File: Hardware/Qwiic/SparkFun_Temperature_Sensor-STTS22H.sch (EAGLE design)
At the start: 28 parts, among them J1 QWIIC_RIGHT_ANGLE, J2 QWIIC_RIGHT_ANGLE, U2 STTS22H

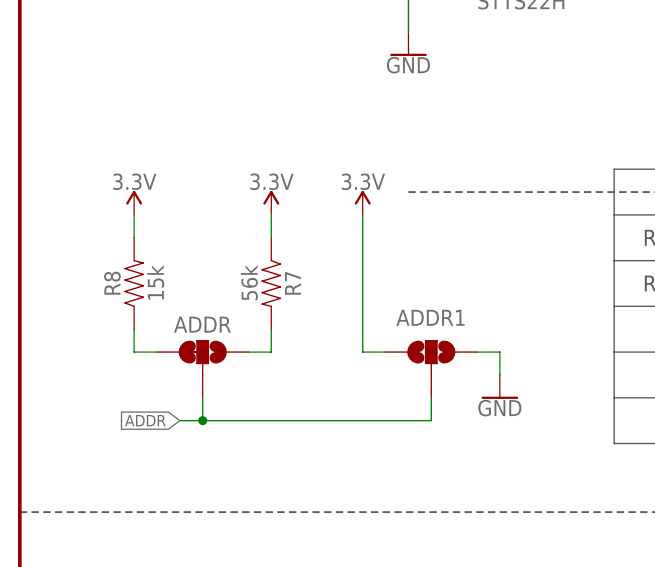
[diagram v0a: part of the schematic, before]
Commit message: Replaces r7 with a 57.6k resistor
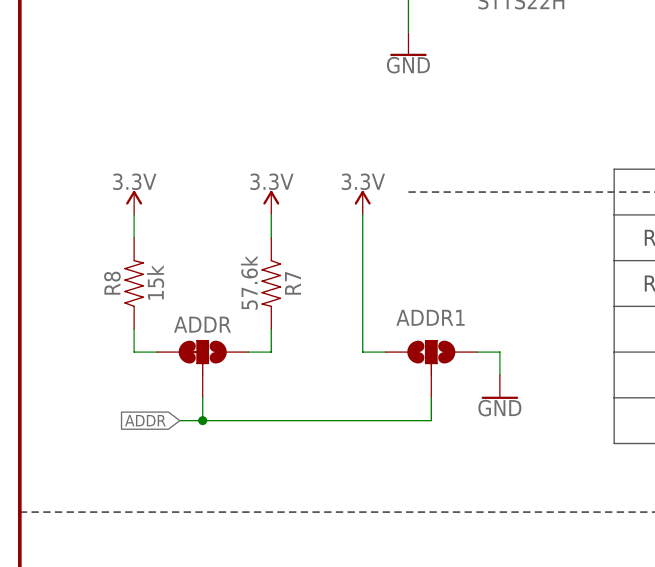
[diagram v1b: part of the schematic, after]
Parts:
- R7: value 56k -> 57.6k; device SparkFun-Resistors:56KOHM -> SparkFun-Resistors:57.6KOHM
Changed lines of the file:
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@@
 <part name="J3" library="SparkFun-Connectors" deviceset="CONN_05" device="NO_SILK"/>
 <part name="ADDR" library="SparkFun-Jumpers" deviceset="JUMPER-SMT_3_1-NC_TRACE" device="_SILK" package3d_urn="urn:adsk.eagle:package:39288/1"/>
-<part name="R7" library="SparkFun-Resistors" deviceset="56KOHM" device="" value="56k"/>
+<part name="R7" library="SparkFun-Resistors" deviceset="57.6KOHM" device="" value="57.6k"/>
 <part name="R8" library="SparkFun-Resistors" deviceset="15KOHM" device="-0603-1/10W-1%" value="15k"/>
 <part name="SUPPLY11" library="SparkFun-PowerSymbols" deviceset="3.3V" device=""/>

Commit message: Adds 56k to R7
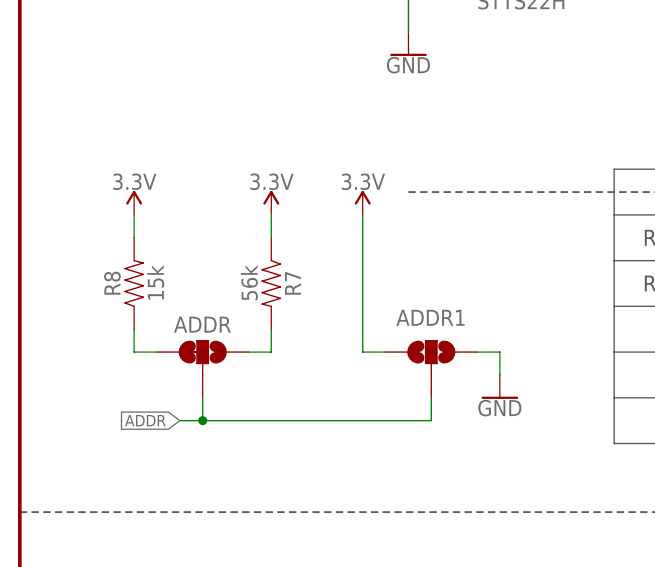
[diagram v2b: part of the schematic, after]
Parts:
- R7: value 57.6k -> 56k; device SparkFun-Resistors:57.6KOHM -> SparkFun-Resistors:56KOHM
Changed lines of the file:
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@@
 <part name="J3" library="SparkFun-Connectors" deviceset="CONN_05" device="NO_SILK"/>
 <part name="ADDR" library="SparkFun-Jumpers" deviceset="JUMPER-SMT_3_1-NC_TRACE" device="_SILK" package3d_urn="urn:adsk.eagle:package:39288/1"/>
-<part name="R7" library="SparkFun-Resistors" deviceset="57.6KOHM" device="" value="57.6k"/>
+<part name="R7" library="SparkFun-Resistors" deviceset="56KOHM" device="" value="56k"/>
 <part name="R8" library="SparkFun-Resistors" deviceset="15KOHM" device="-0603-1/10W-1%" value="15k"/>
 <part name="SUPPLY11" library="SparkFun-PowerSymbols" deviceset="3.3V" device=""/>
